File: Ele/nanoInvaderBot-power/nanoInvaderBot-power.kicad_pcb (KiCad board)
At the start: 2 copper layers, 64 x 40 mm, 10 parts, among them J1 S6B-ZR-SM4A-TF(LF)(SN), J2 S6B-ZR-SM4A-TF(LF)(SN), J3 1746142-1, U3 MP2672AGD-0000-Z

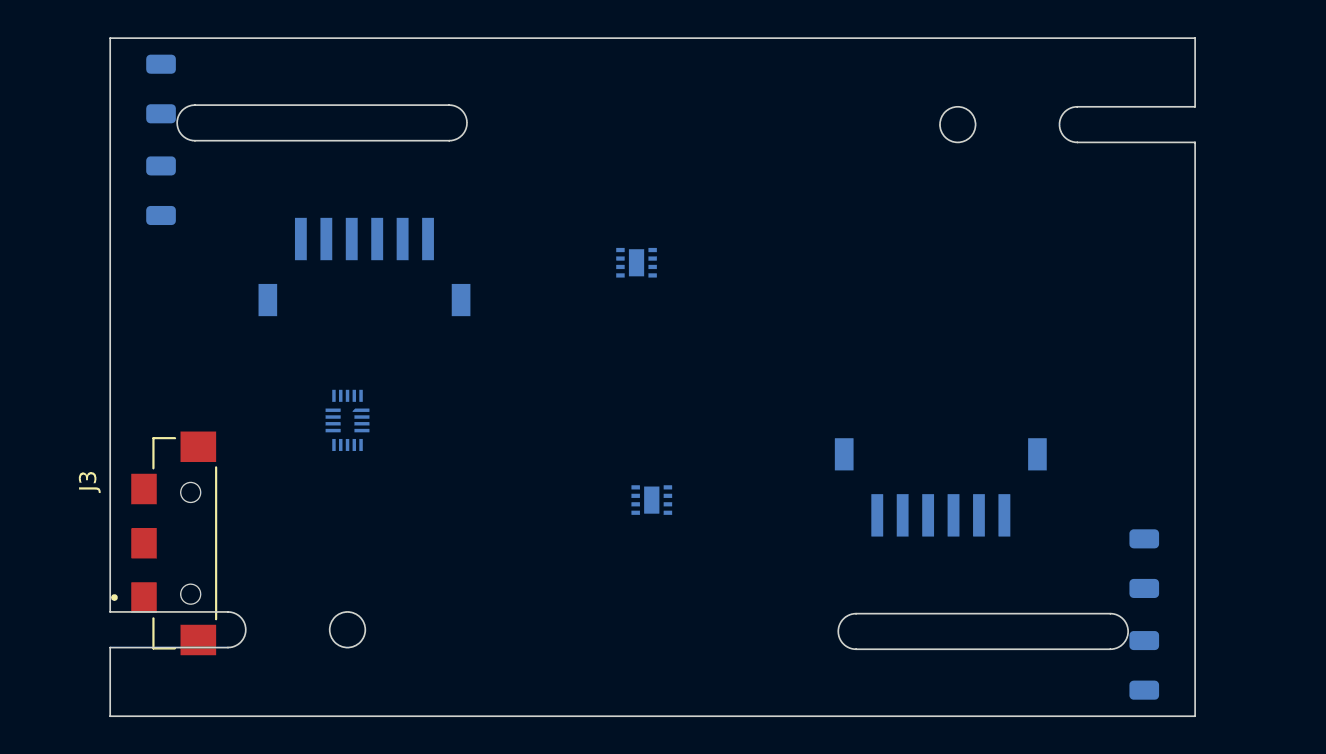
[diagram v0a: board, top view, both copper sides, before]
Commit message: Placed components in power board
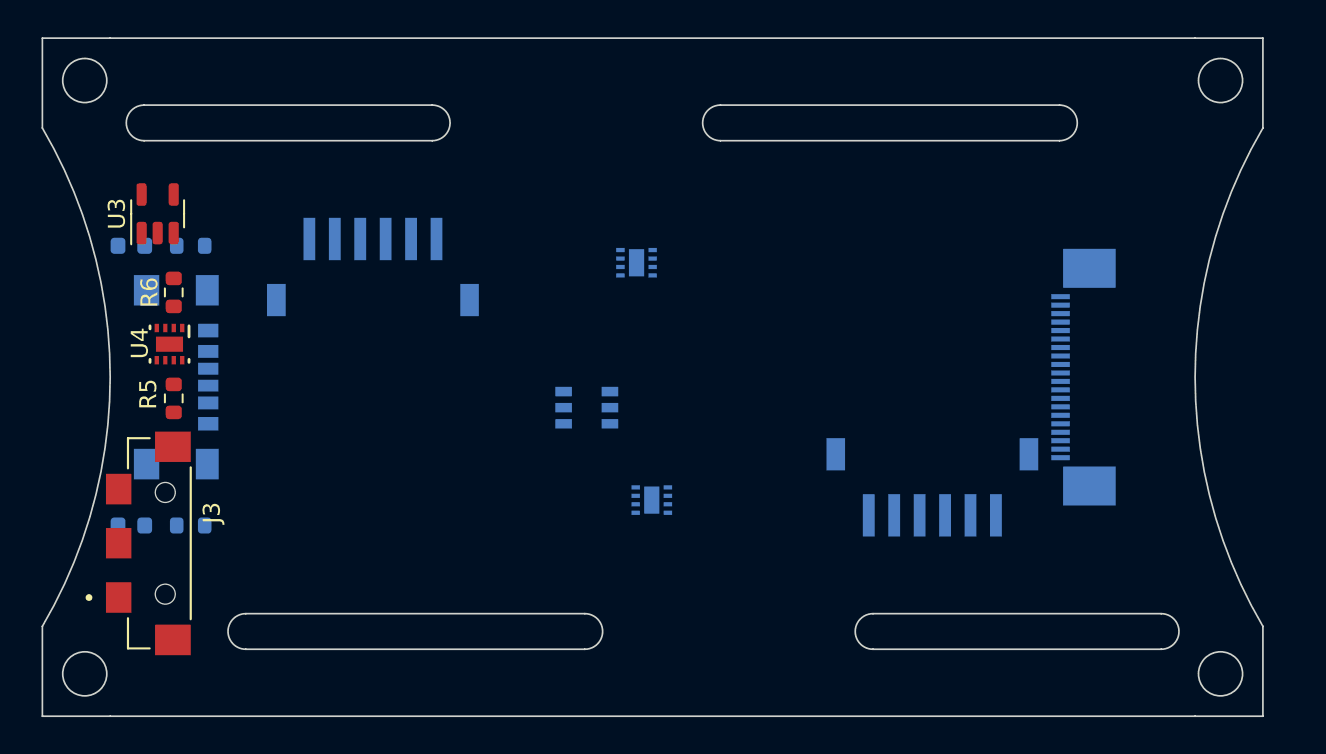
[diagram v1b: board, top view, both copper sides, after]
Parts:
- removed R1, R2, R3, R4: R, Resistor_SMD:R_1206_3216Metric
- added D1: LED, LED_SMD:LED_0603_1608Metric, B.Cu at (119.2, 108.8)
- added D2: LED, LED_SMD:LED_0603_1608Metric, B.Cu at (119.2, 92.2)
- added J4: Conn_01x20, footprints:TE_2-1734839-0, B.Cu at (174.1, 100.0)
- added P1: USB_C_Plug_USB2.0, Connector_USB:USB_C_Receptacle_GCT_USB4135-GF-A_6P_TopMnt_Horizontal, B.Cu at (120.8, 100.0)
- added R5: R, Resistor_SMD:R_0603_1608Metric, F.Cu at (121.8, 101.2)
- added R6: R, Resistor_SMD:R_0603_1608Metric, F.Cu at (121.8, 95.0)
- added R7: R, Resistor_SMD:R_0603_1608Metric, B.Cu at (122.8, 108.8)
- added R8: R, Resistor_SMD:R_0603_1608Metric, B.Cu at (122.8, 92.2)
- added U4: BQ25170DSGR, footprints:BQ25170DSGR_NV, F.Cu at (121.5, 98.0)
- added U5: TLV61048DBVT, footprints:SOT23-6_DBV_TEX, B.Cu at (146.1, 101.8)
- J1, J2: footprint Components:JST_S6B-ZR-SM4A-TF(LF)(SN) -> footprints:JST_S6B-ZR-SM4A-TF(LF)(SN)
- J3: footprint Components:TE_1746142-1 -> footprints:TE_1746142-1
- U3: value MP2672AGD-0000-Z -> ~; footprint Components:QFN-18_MP2672A_MNP -> Package_TO_SOT_SMD:SOT-23-5; moved to F.Cu
- moved U3 16.6 mm to (120.8, 90.4), turned to 90 degrees
- moved J3 1.50 mm to (121.2, 109.8)
- moved J1 0.50 mm to (133.5, 91.8)
- moved J2 0.50 mm to (166.5, 108.2)
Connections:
- J1 pad 1: /MOTOR1_B -> /MOTOR1_A
- J1 pad 2: unconnected-(J1-Pad2) -> /GND
- J1 pad 3: unconnected-(J1-Pad3) -> /MOTOR1_C1
- J1 pad 4: unconnected-(J1-Pad4) -> /MOTOR1_C2
- J1 pad 5: unconnected-(J1-Pad5) -> /3V3
- J1 pad 6: /MOTOR1_A -> /MOTOR1_B
- J1 pad SH1: Net-(J1-SHIELD-PadSH1) -> unconnected-(J1-SHIELD-PadSH1)
- J1 pad SH2: Net-(J1-SHIELD-PadSH1) -> unconnected-(J1-SHIELD-PadSH1)
- J2 pad 1: /MOTOR2_B -> /MOTOR2_A
- J2 pad 2: unconnected-(J2-Pad2) -> /GND
- J2 pad 3: unconnected-(J2-Pad3) -> /MOTOR2_C1
- J2 pad 4: unconnected-(J2-Pad4) -> /MOTOR2_C2
- J2 pad 5: unconnected-(J2-Pad5) -> /3V3
- J2 pad 6: /MOTOR2_A -> /MOTOR2_B
- J2 pad SH1: Net-(J2-SHIELD-PadSH1) -> unconnected-(J2-SHIELD-PadSH1)
- J2 pad SH2: Net-(J2-SHIELD-PadSH1) -> unconnected-(J2-SHIELD-PadSH1)
- U1 pad 1: /VSYS -> /12V
- U2 pad 1: /VSYS -> /12V
- U3 pad 1: unconnected-(U3-IN-Pad1) -> /VBATT
- U3 pad 2: unconnected-(U3-SW-Pad2) -> /GND
- U3 pad 3: unconnected-(U3-BST-Pad3) -> /VBATT
- U3 pad 5: unconnected-(U3-ISET-Pad5) -> /VSYS
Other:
- board size 64 x 40 mm -> 72 x 40 mm

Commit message: Intermediate state -power layer almost done
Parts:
- removed P1: USB_C_Plug_USB2.0, Connector_USB:USB_C_Receptacle_GCT_USB4135-GF-A_6P_TopMnt_Horizontal
- added C1: C, Capacitor_SMD:C_1210_3225Metric, B.Cu at (140.5, 102.2)
- added C10: C, Capacitor_SMD:C_0603_1608Metric, F.Cu at (118.8, 87.2)
- added C2: C, Capacitor_SMD:C_1210_3225Metric, B.Cu at (157.5, 98.0)
- added C3: C, Capacitor_SMD:C_1210_3225Metric, B.Cu at (156.2, 93.2)
- added C4: C, Capacitor_SMD:C_0603_1608Metric, B.Cu at (153.0, 92.2)
- added C5: C, Capacitor_SMD:C_1210_3225Metric, B.Cu at (145.5, 106.2)
- added C6: C, Capacitor_SMD:C_0603_1608Metric, B.Cu at (146.8, 108.8)
- added C7: C, Capacitor_SMD:C_0603_1608Metric, F.Cu at (116.7, 96.8)
- added C8: C, Capacitor_SMD:C_0603_1608Metric, F.Cu at (116.7, 99.3)
- added C9: C, Capacitor_SMD:C_0603_1608Metric, F.Cu at (118.0, 89.8)
- added D3: D, footprints:SDO_B120AF_DIO, B.Cu at (151.5, 98.0)
- added L1: L, footprints:IND_SWPA5040S_SNL, B.Cu at (145.2, 101.8)
- added R1: R, Resistor_SMD:R_0402_1005Metric, F.Cu at (122.2, 93.2)
- added R10: R, Resistor_SMD:R_0402_1005Metric, B.Cu at (155.5, 100.2)
- added R9: R, Resistor_SMD:R_0402_1005Metric, B.Cu at (157.8, 100.2)
- added SW1: SW_SPDT, Button_Switch_SMD:SW_SPDT_PCM12, B.Cu at (120.0, 100.0)
- D1, D2: footprint LED_SMD:LED_0603_1608Metric -> Resistor_SMD:R_0402_1005Metric
- R5, R6, R7, R8: footprint Resistor_SMD:R_0603_1608Metric -> Resistor_SMD:R_0402_1005Metric
- moved U5 4.24 mm to (150.2, 102.8), turned to -90 degrees
- moved U1 1.25 mm to (149.0, 92.0), turned to 0 degrees
- moved U2 1.21 mm to (151.0, 107.8)
- moved D2 1.00 mm to (119.2, 91.2)
- moved R8 1.00 mm to (122.8, 91.2)
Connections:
- J1 pad 3: /MOTOR1_C1 -> /MOTOR1_ENC1
- J1 pad 4: /MOTOR1_C2 -> /MOTOR1_ENC2
- J1 pad SH1: unconnected-(J1-SHIELD-PadSH1) -> /GND
- J1 pad SH2: unconnected-(J1-SHIELD-PadSH1) -> /GND
- J2 pad 3: /MOTOR2_C1 -> /MOTOR2_ENC1
- J2 pad 4: /MOTOR2_C2 -> /MOTOR2_ENC2
- J2 pad SH1: unconnected-(J2-SHIELD-PadSH1) -> /GND
- J2 pad SH2: unconnected-(J2-SHIELD-PadSH1) -> /GND
- J4 pad 1: unconnected-(J4-Pin_1-Pad1) -> /VSYS
- J4 pad 10: unconnected-(J4-Pin_10-Pad10) -> /SYS_EN
- J4 pad 11: unconnected-(J4-Pin_11-Pad11) -> /3V3
- J4 pad 12: unconnected-(J4-Pin_12-Pad12) -> /MOTOR2_ENC1
- J4 pad 13: unconnected-(J4-Pin_13-Pad13) -> /MOTOR2_ENC2
- J4 pad 14: unconnected-(J4-Pin_14-Pad14) -> /MOTOR2_B_MCU
- J4 pad 15: unconnected-(J4-Pin_15-Pad15) -> /MOTOR2_A_MCU
- J4 pad 16: unconnected-(J4-Pin_16-Pad16) -> /MOTOR2_EN_MCU
- J4 pad 17: unconnected-(J4-Pin_17-Pad17) -> /GND
- J4 pad 18: unconnected-(J4-Pin_18-Pad18) -> /GND
- J4 pad 19: unconnected-(J4-Pin_19-Pad19) -> /VUSB
- J4 pad 2: unconnected-(J4-Pin_2-Pad2) -> /VSYS
- J4 pad 20: unconnected-(J4-Pin_20-Pad20) -> /VUSB
- J4 pad 3: unconnected-(J4-Pin_3-Pad3) -> /GND
- J4 pad 4: unconnected-(J4-Pin_4-Pad4) -> /GND
- J4 pad 5: unconnected-(J4-Pin_5-Pad5) -> /MOTOR1_B_MCU
- J4 pad 6: unconnected-(J4-Pin_6-Pad6) -> /MOTOR1_A_MCU
- J4 pad 7: unconnected-(J4-Pin_7-Pad7) -> /MOTOR1_EN_MCU
- J4 pad 8: unconnected-(J4-Pin_8-Pad8) -> /MOTOR1_ENC1
- J4 pad 9: unconnected-(J4-Pin_9-Pad9) -> /MOTOR1_ENC2
- U3 pad 3: /VBATT -> /SYS_EN
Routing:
- net /3V3: track 0.00 -> 107.8 mm, vias 0 -> 6
- net /VSYS: track 0.00 -> 100.2 mm, vias 0 -> 2
- net /GND: track 0.00 -> 78.4 mm, vias 0 -> 10
- net /VUSB: track 0.00 -> 75.5 mm, vias 0 -> 1
- net /SYS_EN: track 0.00 -> 75.4 mm, vias 0 -> 3
- net /MOTOR1_ENC2: track 0.00 -> 47.3 mm
- net /MOTOR1_ENC1: track 0.00 -> 45.9 mm
- net /VBATT: track 0.00 -> 40.1 mm, vias 0 -> 2
- net /MOTOR2_EN_MCU: track 0.00 -> 39.8 mm
- net /MOTOR2_A_MCU: track 0.00 -> 38.2 mm
- net /MOTOR2_B_MCU: track 0.00 -> 36.6 mm
- net /12V: track 0.00 -> 36.2 mm, vias 0 -> 4
- net /MOTOR1_EN_MCU: track 0.00 -> 28.0 mm
- net /MOTOR1_A_MCU: track 0.00 -> 28.0 mm
- net /MOTOR1_B_MCU: track 0.00 -> 28.0 mm
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- added copper zone on B.Cu, net /GND

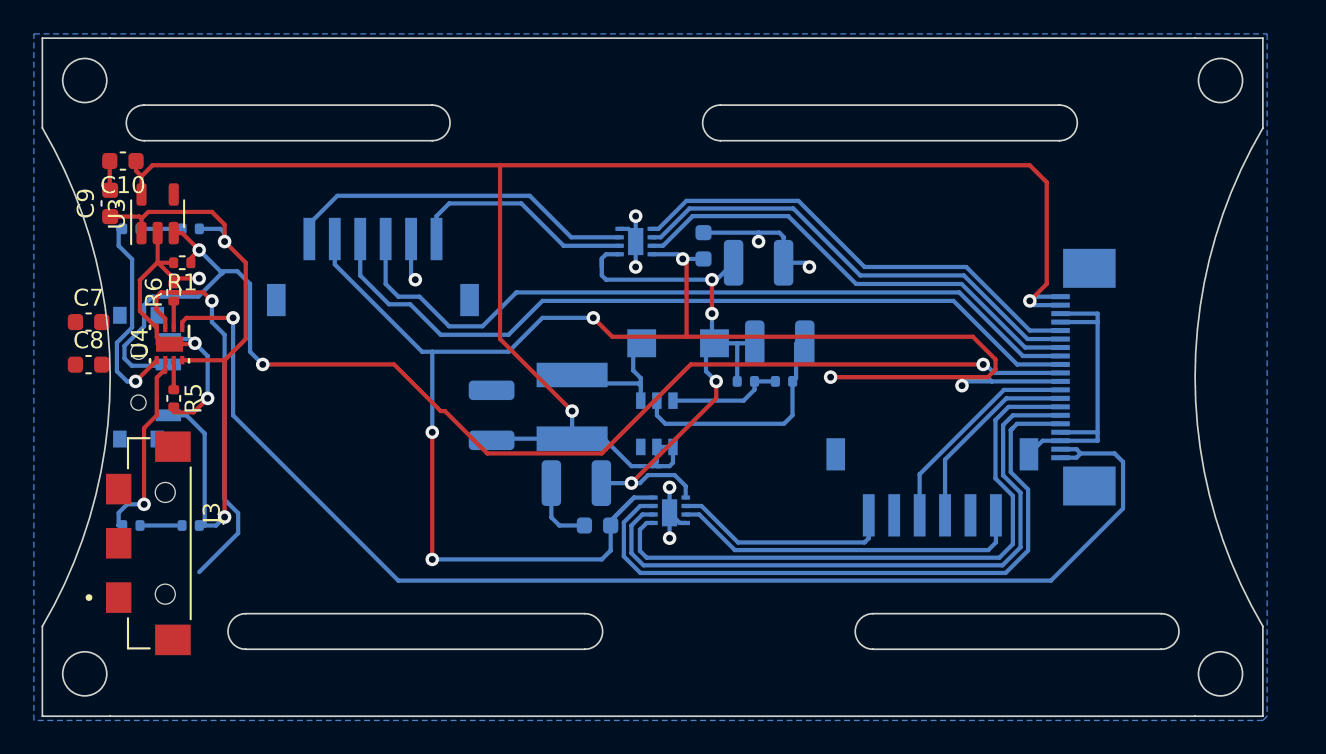
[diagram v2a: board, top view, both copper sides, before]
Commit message: Power side done, logic side cleanup
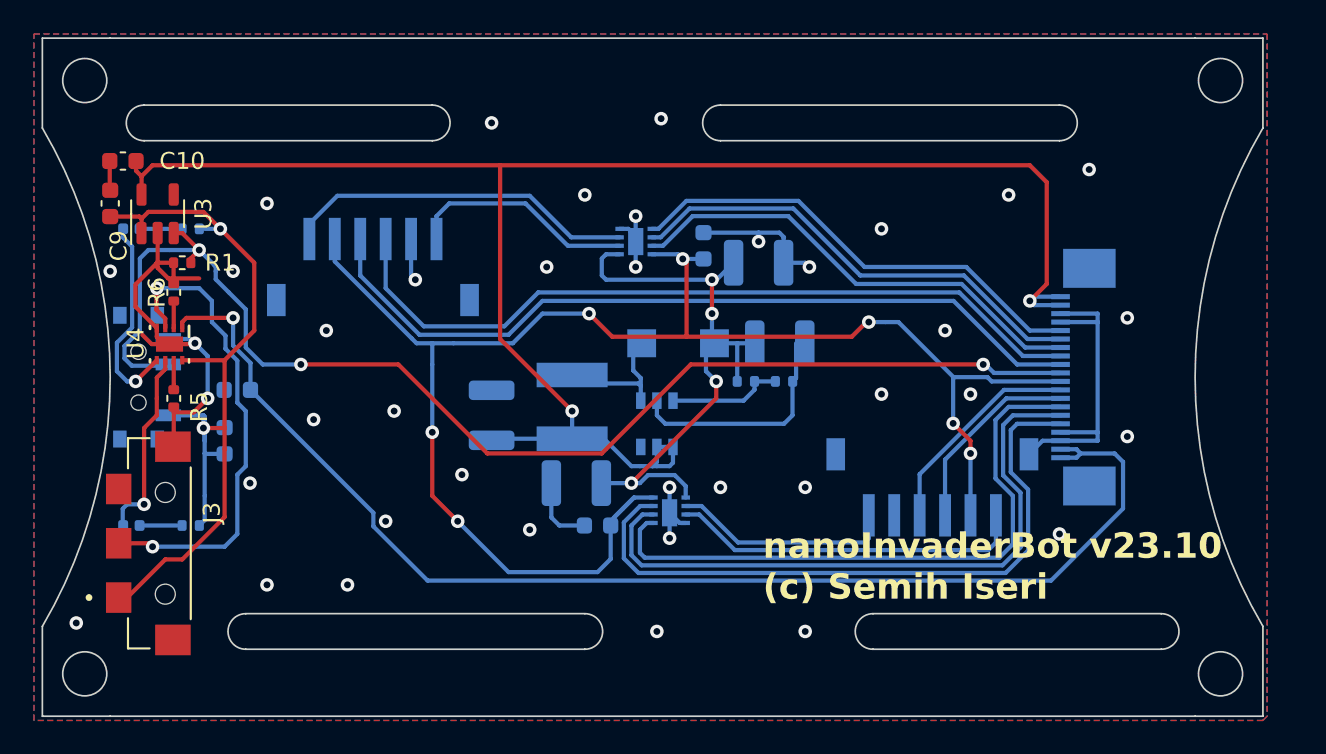
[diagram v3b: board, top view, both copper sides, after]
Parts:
- C7, C8: moved to B.Cu
- D1, D2: footprint Resistor_SMD:R_0402_1005Metric -> LED_SMD:LED_0402_1005Metric
- moved C7 9.64 mm to (125.5, 100.8), turned to 180 degrees
- moved C8 9.20 mm to (124.8, 103.8), turned to 90 degrees
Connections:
- J3 pad 1: unconnected-(J3-Pad1) -> /VBATT
- J3 pad 2: unconnected-(J3-Pad2) -> /TBATT
- J3 pad 3: unconnected-(J3-Pad3) -> /GND
- J3 pad SH1: unconnected-(J3-SHIELD1-PadSH1) -> /GND
- J3 pad SH2: unconnected-(J3-SHIELD2-PadSH2) -> /GND
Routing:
- net /3V3: track 107.8 -> 94.3 mm, vias 6 -> 7
- net /VBATT: track 40.1 -> 50.5 mm
- net /GND: track 78.4 -> 84.3 mm, vias 10 -> 39
- net /TBATT: track 23.6 -> 28.3 mm, vias 1 -> 2
- net /VUSB: track 75.5 -> 74.5 mm
- net /12V: track 36.2 -> 35.7 mm
- added copper zone on F.Cu, net /GND
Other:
- board text added: "nanoInvaderBot v23.10 (c) Semih Iseri"

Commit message: Intermediate state after v23.10
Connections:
- J4 pad 10: /SYS_EN -> /3V3
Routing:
- net /SYS_EN: track 75.6 -> 15.6 mm, vias 3 -> 1
- net /3V3: track 94.3 -> 96.4 mm
